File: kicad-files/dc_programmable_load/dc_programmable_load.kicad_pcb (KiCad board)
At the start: 2 copper layers, 14 parts, among them J1 DC Jack 12V, J2 Conn_01x03_Socket, Q1 IRF3205, U2 LM317_SOT-223, U4 LM358DR

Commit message: version 1 of the PCB
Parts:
- added C1: 10uF, Capacitor_SMD:C_0805_2012Metric, F.Cu at (166.0, 99.0)
- added C10: 100nF, Capacitor_SMD:C_0603_1608Metric, F.Cu at (161.0, 92.5)
- added C2: 10uF, Capacitor_SMD:C_0805_2012Metric, F.Cu at (138.0, 98.5)
- added C3: 100nF, Capacitor_SMD:C_0603_1608Metric, F.Cu at (149.0, 66.5)
- added C4: 10uF, Capacitor_SMD:C_0805_2012Metric, F.Cu at (157.5, 67.5)
- added C5: 100nF, Capacitor_SMD:C_0603_1608Metric, F.Cu at (129.5, 92.5)
- added C6: 1uF, Capacitor_SMD:C_0805_2012Metric, F.Cu at (131.5, 89.5)
- added C7: 100nF, Capacitor_SMD:C_0603_1608Metric, F.Cu at (142.0, 93.0)
- added C8: 1uF, Capacitor_SMD:C_0805_2012Metric, F.Cu at (144.0, 91.0)
- added C9: 100nF, Capacitor_SMD:C_0603_1608Metric, F.Cu at (161.5, 85.5)
- added J3: Conn_01x04_Socket, Connector_PinHeader_2.00mm:PinHeader_1x04_P2.00mm_Vertical, F.Cu at (154.5, 98.5)
- added J4: Conn_01x04_Socket, Connector_PinHeader_2.00mm:PinHeader_1x04_P2.00mm_Vertical, F.Cu at (167.0, 80.0)
- added J5: Conn_01x01_Socket, Connector_PinHeader_2.00mm:PinHeader_1x01_P2.00mm_Vertical, F.Cu at (150.5, 98.5)
- added J6: Conn_01x01_Socket, Connector_PinHeader_2.00mm:PinHeader_1x01_P2.00mm_Vertical, F.Cu at (143.5, 98.5)
- added R5: 10k, Resistor_SMD:R_0805_2012Metric, F.Cu at (145.0, 74.0)
- added RV1: R_Potentiometer, Potentiometer_SMD:Potentiometer_Bourns_3314S_Horizontal, F.Cu at (152.0, 81.5)
- added Shunt1: 1, Resistor_SMD:R_2512_6332Metric, F.Cu at (136.0, 80.0)
- moved A1 45.7 mm to (130.4, 117.1), turned to 90 degrees
- moved R6 37.7 mm to (143.5, 78.0), turned to 90 degrees
- moved TempSnsr1 29.5 mm to (156.1, 94.2)
- moved R4 28.9 mm to (142.5, 83.9), turned to 90 degrees
- moved Q1 27.0 mm to (140.5, 69.5), turned to 180 degrees
- moved J2 26.4 mm to (167.0, 95.0), turned to 180 degrees
- moved R3 25.1 mm to (146.5, 86.5)
- moved R1 24.4 mm to (128.5, 79.5), turned to -90 degrees
- moved R2 19.6 mm to (128.5, 87.5), turned to -90 degrees
- moved U2 19.1 mm to (151.5, 71.0), turned to 180 degrees
- moved J1 18.3 mm to (160.5, 71.5), turned to 90 degrees
- moved ADC1 15.6 mm to (137.5, 91.5), turned to 180 degrees
- moved DAC1 15.3 mm to (146.6, 94.1), turned to -90 degrees
- moved U4 3.11 mm to (157.0, 89.0)
- renumbered Temp_Snsr1 to TempSnsr1
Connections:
- net +5V renamed /Power Supply
- U2 pad 1: unconnected-(U2-ADJ-Pad1) -> Net-(U2-ADJ)
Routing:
- net /Power Supply: track 0.00 -> 51.7 mm
- net /sda: track 0.00 -> 41.9 mm, vias 0 -> 4
- net /5V: track 0.00 -> 36.4 mm, vias 0 -> 2
- net /scl: track 0.00 -> 36.4 mm, vias 0 -> 2
- net /12V: track 0.00 -> 26.4 mm
- net /3v3: track 0.00 -> 26.0 mm, vias 0 -> 2
- net /A0: track 0.00 -> 26.0 mm
- net /A2: track 0.00 -> 17.7 mm
- net /opamp_output: track 0.00 -> 16.6 mm
- net Net-(U2-ADJ): track 0.00 -> 15.2 mm
- net Net-(U4-1IN-): track 0.00 -> 14.0 mm
- net Net-(J2-Pin_3): track 0.00 -> 10.7 mm
- net Net-(J2-Pin_2): track 0.00 -> 10.1 mm
- net Net-(J2-Pin_1): track 0.00 -> 9.52 mm
- net Net-(Q1-G): track 0.00 -> 8.83 mm
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- added copper zone on B.Cu, net GND
- added copper zone on F.Cu, net GND
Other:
- board outline added: 47 x 53.5 mm

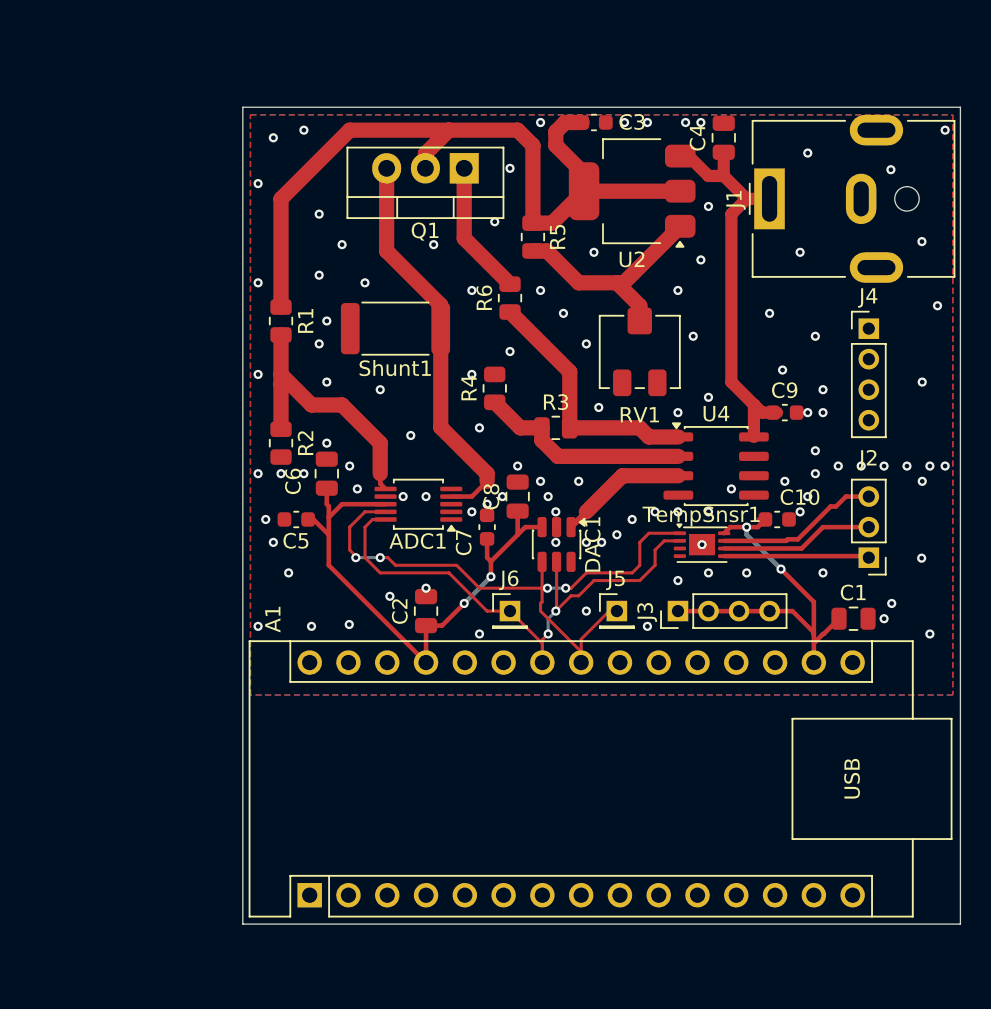
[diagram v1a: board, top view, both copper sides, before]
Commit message: revised board and changed to buck
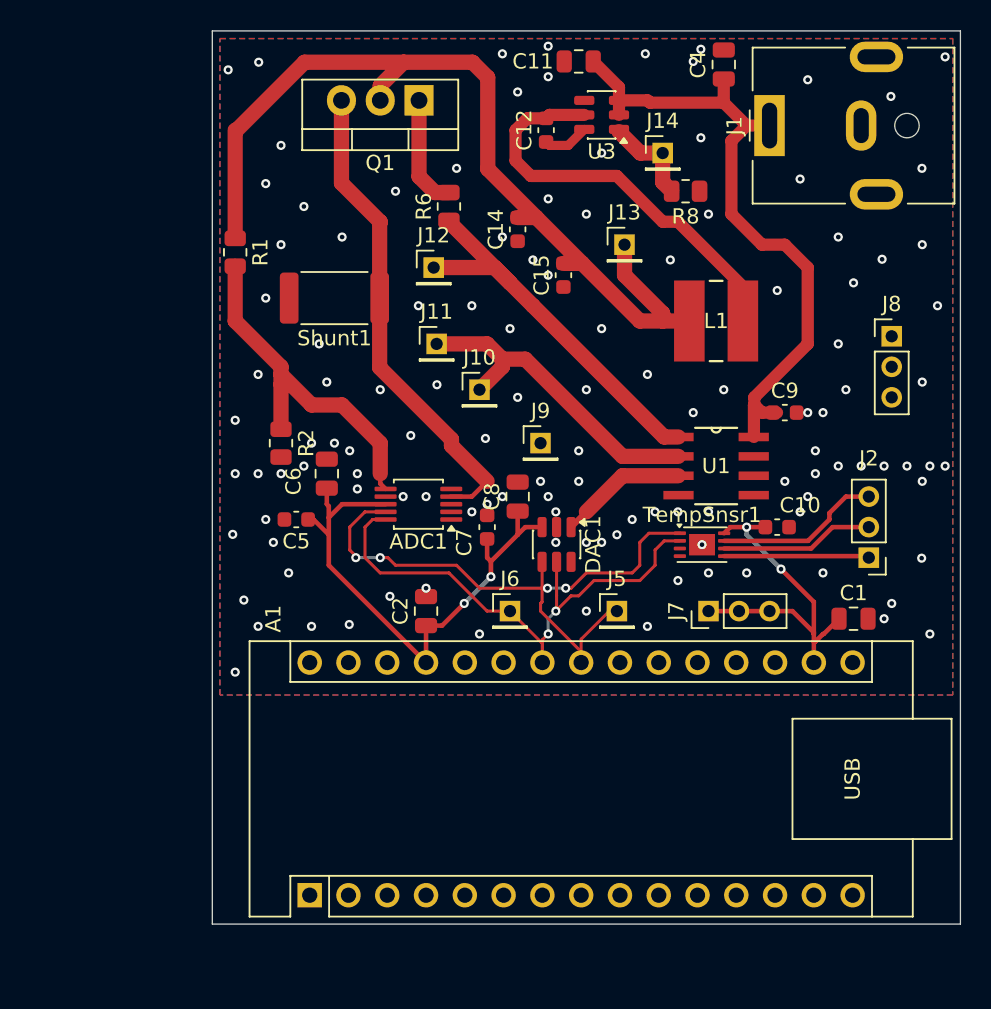
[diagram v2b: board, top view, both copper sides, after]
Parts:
- removed C3: 100nF, Capacitor_SMD:C_0603_1608Metric
- removed J3, J4: Conn_01x04_Socket, Connector_PinHeader_2.00mm:PinHeader_1x04_P2.00mm_Vertical
- removed R3: 4.7K, Resistor_SMD:R_0805_2012Metric
- removed R4: 10K, Resistor_SMD:R_0805_2012Metric
- removed R5: 10k, Resistor_SMD:R_0805_2012Metric
- removed RV1: R_Potentiometer, Potentiometer_SMD:Potentiometer_Bourns_3314S_Horizontal
- removed U2: LM317_SOT-223, Package_TO_SOT_SMD:SOT-223-3_TabPin2
- removed U4: LM358DR, Package_SO:SOIC-8_3.9x4.9mm_P1.27mm
- added C11: 10uF, Capacitor_SMD:C_0805_2012Metric, F.Cu at (148.0, 62.5)
- added C12: 100nF, Capacitor_SMD:C_0603_1608Metric, F.Cu at (145.9, 67.0)
- added C14: 22uF, Capacitor_SMD:C_0603_1608Metric, F.Cu at (144.0, 73.5)
- added C15: 22uF, Capacitor_SMD:C_0603_1608Metric, F.Cu at (147.0, 76.5)
- added J10: Conn_01x01_Socket, Connector_PinHeader_2.00mm:PinHeader_1x01_P2.00mm_Vertical, F.Cu at (141.5, 84.0)
- added J11: Conn_01x01_Socket, Connector_PinHeader_2.00mm:PinHeader_1x01_P2.00mm_Vertical, F.Cu at (138.7, 81.0)
- added J12: Conn_01x01_Socket, Connector_PinHeader_2.00mm:PinHeader_1x01_P2.00mm_Vertical, F.Cu at (138.5, 76.0)
- added J13: Conn_01x01_Socket, Connector_PinHeader_2.00mm:PinHeader_1x01_P2.00mm_Vertical, F.Cu at (151.0, 74.5)
- added J14: Conn_01x01_Socket, Connector_PinHeader_2.00mm:PinHeader_1x01_P2.00mm_Vertical, F.Cu at (153.5, 68.5)
- added J7: Conn_01x03_Socket, Connector_PinHeader_2.00mm:PinHeader_1x03_P2.00mm_Vertical, F.Cu at (156.5, 98.5)
- added J8: Conn_01x03_Socket, Connector_PinHeader_2.00mm:PinHeader_1x03_P2.00mm_Vertical, F.Cu at (168.5, 80.5)
- added J9: Conn_01x01_Socket, Connector_PinHeader_2.00mm:PinHeader_1x01_P2.00mm_Vertical, F.Cu at (145.5, 87.5)
- added L1: SRR4028-4R7Y, SRR4028:IND_BOURNS_SRR4028, F.Cu at (157.0, 79.5)
- added R8: 10k, Resistor_SMD:R_0805_2012Metric, F.Cu at (155.0, 71.0)
- added U1: LM358DR, LM358DR:D8, F.Cu at (157.0, 89.0)
- added U3: AP63200WU, Package_TO_SOT_SMD:TSOT-23-6, F.Cu at (149.5, 66.0)
- moved R6 7.21 mm to (139.5, 72.0)
- moved R1 5.41 mm to (125.5, 75.0)
- moved Q1 5.34 mm to (137.5, 65.0)
- moved C4 4.80 mm to (157.5, 62.7)
- moved J1 4.80 mm to (160.5, 66.7)
- moved Shunt1 4.47 mm to (132.0, 78.0)
- moved C10 0.50 mm to (161.0, 93.0)
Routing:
- net Net-(U3-SW): track 0.00 -> 27.0 mm
- net Net-(J10-Pin_1): track 0.00 -> 21.5 mm
- net /12V: track 26.4 -> 42.7 mm
- net Net-(U2-ADJ): track 15.2 -> 0.00 mm
- net Net-(U4-1IN-): track 14.0 -> 0.00 mm
- net /opamp_output: track 16.6 -> 26.4 mm
- net /Power Supply: track 51.7 -> 60.8 mm
- net Net-(J14-Pin_1): track 0.00 -> 6.19 mm
- net /A2: track 17.7 -> 23.4 mm
- net /A0: track 26.0 -> 31.7 mm
- net Net-(U3-BST): track 0.00 -> 3.03 mm
- net /3v3: track 26.0 -> 23.4 mm
- net Net-(Q1-G): track 8.83 -> 7.38 mm
- net GND: vias 107 -> 121
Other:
- board size 47 x 53.5 mm -> 49 x 58.5 mm
